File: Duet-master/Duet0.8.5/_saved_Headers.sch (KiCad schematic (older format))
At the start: 19 parts, among them J10 GND V_IN, J11 GND V_IN, J12 E1 TEMP, J13 Probe, J6 EXPANSION, J7 PanelDUE, J8 POWER IN, J9 5V_PS, U10 USB_3.0_Receptacle, U13 USB_3.0_Receptacle_4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

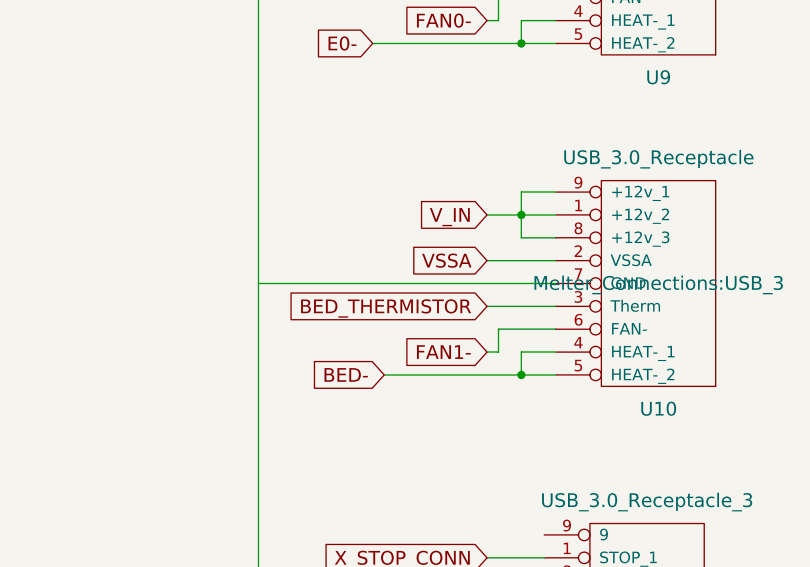
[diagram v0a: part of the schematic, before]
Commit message: USB 3 receptacles!
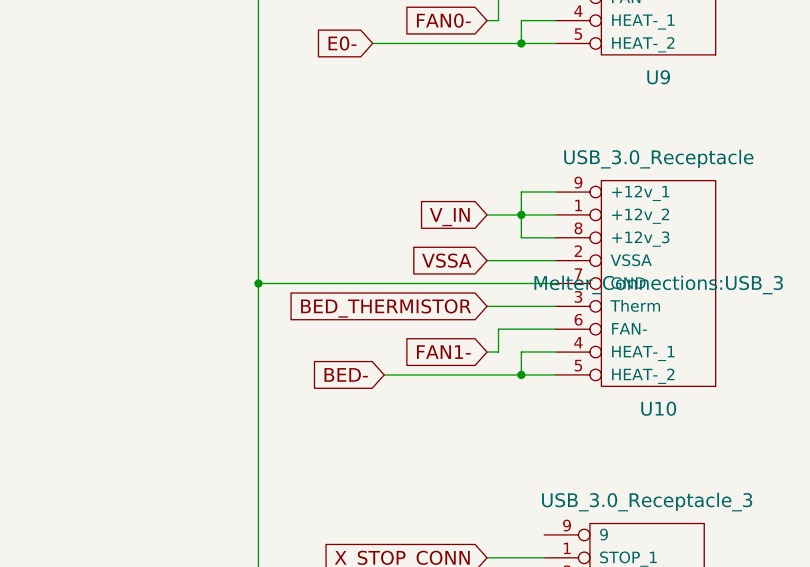
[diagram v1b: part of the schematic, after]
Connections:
- net GND: now also U10.7 (GND)
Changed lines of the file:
@@
 Connection ~ 12950 5600
-Wire Wire Line
-	11800 5900 13100 5900
 Wire Wire Line
 	13100 6000 12800 6000
@@
 Wire Wire Line
 	13100 1700 12600 1700
-Wire Wire Line
-	13100 4450 11800 4450
 Wire Wire Line
 	13100 4550 12800 4550
@@
 Wire Wire Line
 	9400 8950 9350 8950
+Wire Wire Line
+	13100 5900 11800 5900
+Connection ~ 11800 5900
+Wire Wire Line
+	13100 4450 11800 4450
 $EndSCHEMATC
